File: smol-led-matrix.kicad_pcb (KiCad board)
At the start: 4 copper layers, 46.4 x 20.4 mm, 320 parts, among them J1 USB_C_Receptacle_USB2.0, J2 TagConnect_TC2030_SWD, Q1 FS8205, Q2 AO3401A, SW1 SW_Push, SW2 SW_Push, U1 STM32L433CBTx, U2 TP4054, U3 DW01+G, U4 XC6206P332MR

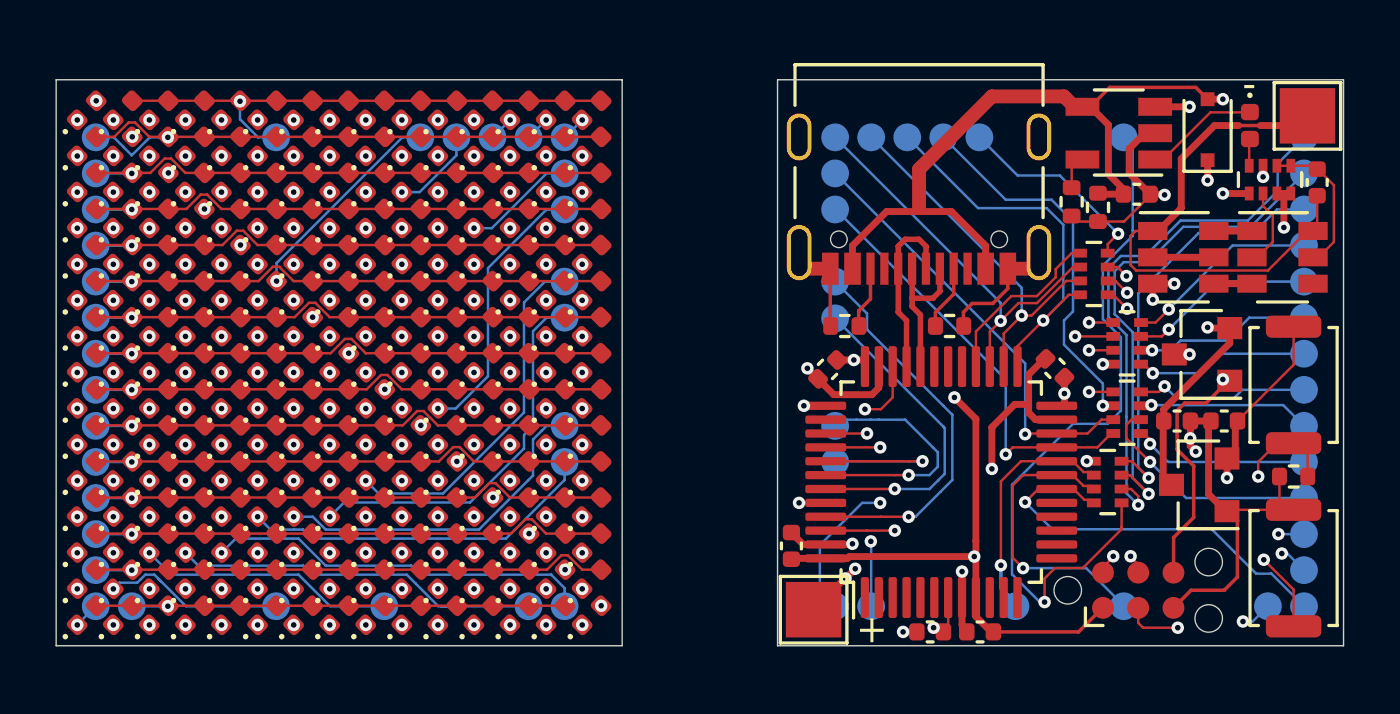
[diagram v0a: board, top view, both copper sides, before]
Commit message: Embed battery pads in plane for added mchanica rigidity
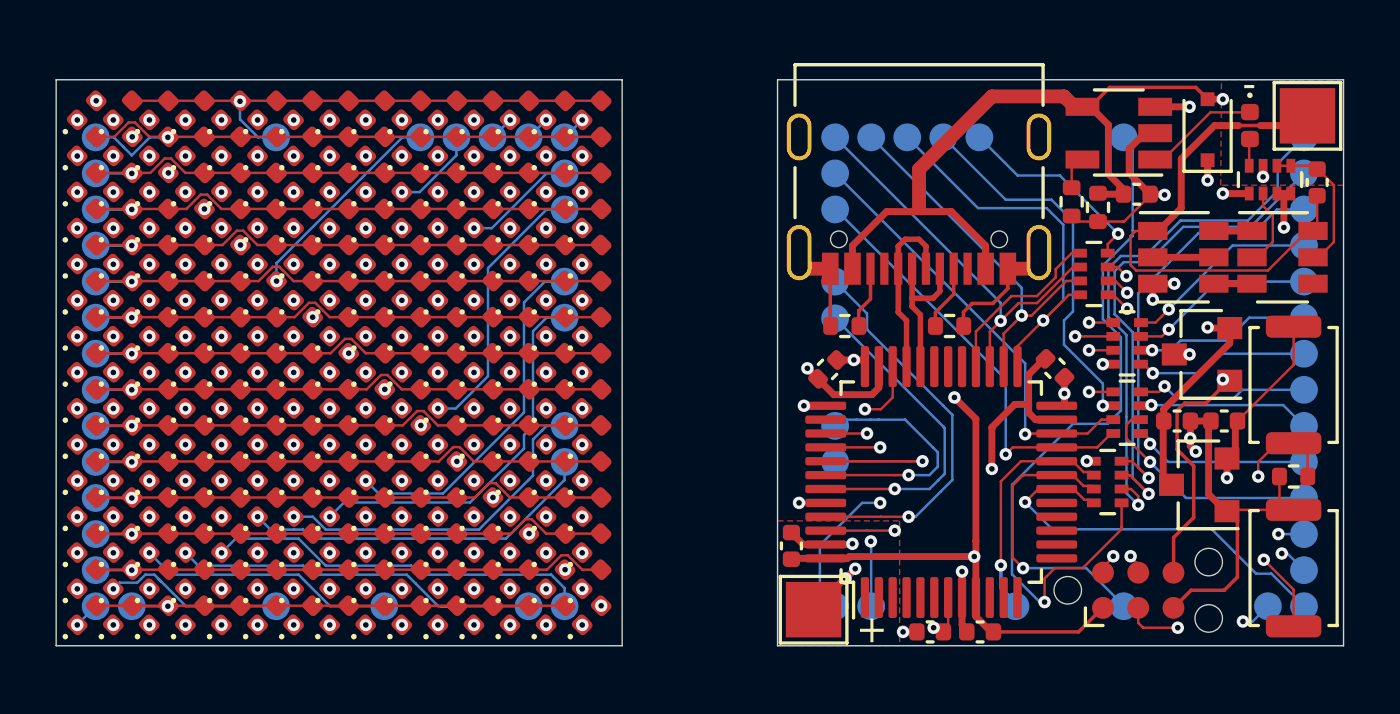
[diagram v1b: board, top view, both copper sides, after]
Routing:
- added copper zone on F.Cu, net +BATT
- added copper zone on F.Cu, net /Power/BAT-
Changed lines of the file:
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@@
     (user_trace_width 0.5)
     (trace_clearance 0.09)
-    (zone_clearance 0.508)
+    (zone_clearance 0.127)
     (zone_45_only no)
     (trace_min 0.09)
@@
       )
     )
+  )
+  (zone (net 66) (net_name +BATT) (layer F.Cu) (hatch edge 0.508)
+    (priority 10)
+    (connect_pads yes (clearance 0.127))
+    (min_thickness 0.127)
+    (fill yes (arc_segments 32) (thermal_gap 0.508) (thermal_bridge_width 0.508))
+    (polygon
+      (pts
+        (xy 129.975 117.975) (xy 125.575 117.975) (xy 125.575 113.475) (xy 129.975 113.475)
+      )
+    )
+  )
+  (zone (net 69) (net_name /Power/BAT-) (layer F.Cu) (hatch edge 0.508)
+    (priority 10)
+    (connect_pads yes (clearance 0.127))
+    (min_thickness 0.127)
+    (fill yes (arc_segments 32) (thermal_gap 0.508) (thermal_bridge_width 0.508))
+    (polygon
+      (pts
+        (xy 141.575 97.575) (xy 145.975 97.575) (xy 145.975 101.375) (xy 141.55 101.375)
+      )
+    )

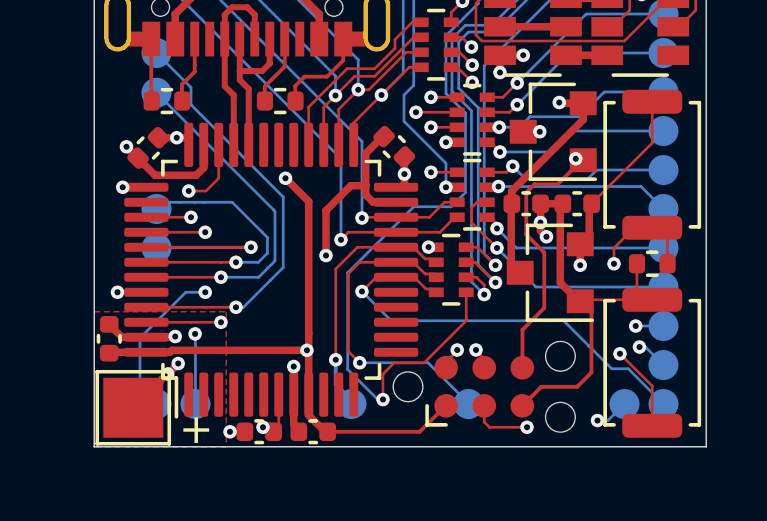
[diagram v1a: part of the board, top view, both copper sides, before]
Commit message: Bump up charge current to 45mA
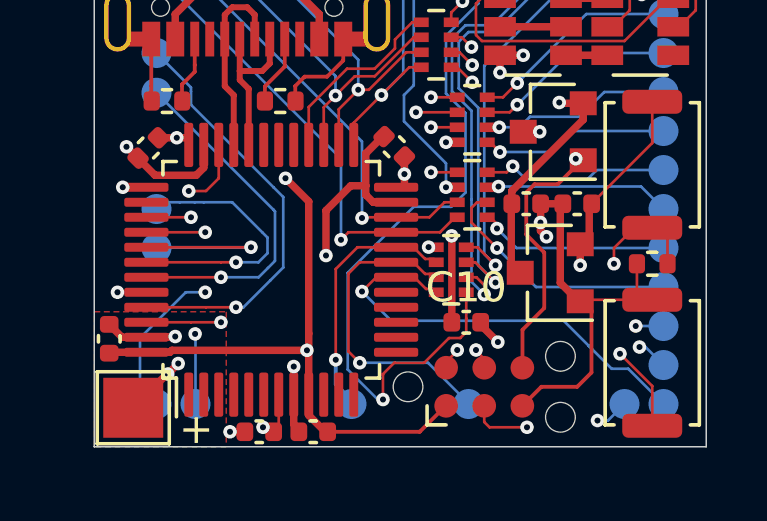
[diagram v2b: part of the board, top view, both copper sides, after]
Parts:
- added C10: 10uF, Capacitor_SMD:C_0402_1005Metric, F.Cu at (138.0, 113.8)
- R1: value 27kR -> 22kR
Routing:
- net GND: track 46.6 -> 49.4 mm, vias 11 -> 12
- net /A14: track 35.7 -> 37.0 mm
- net +3V3: track 46.9 -> 48.1 mm, vias 5 -> 6

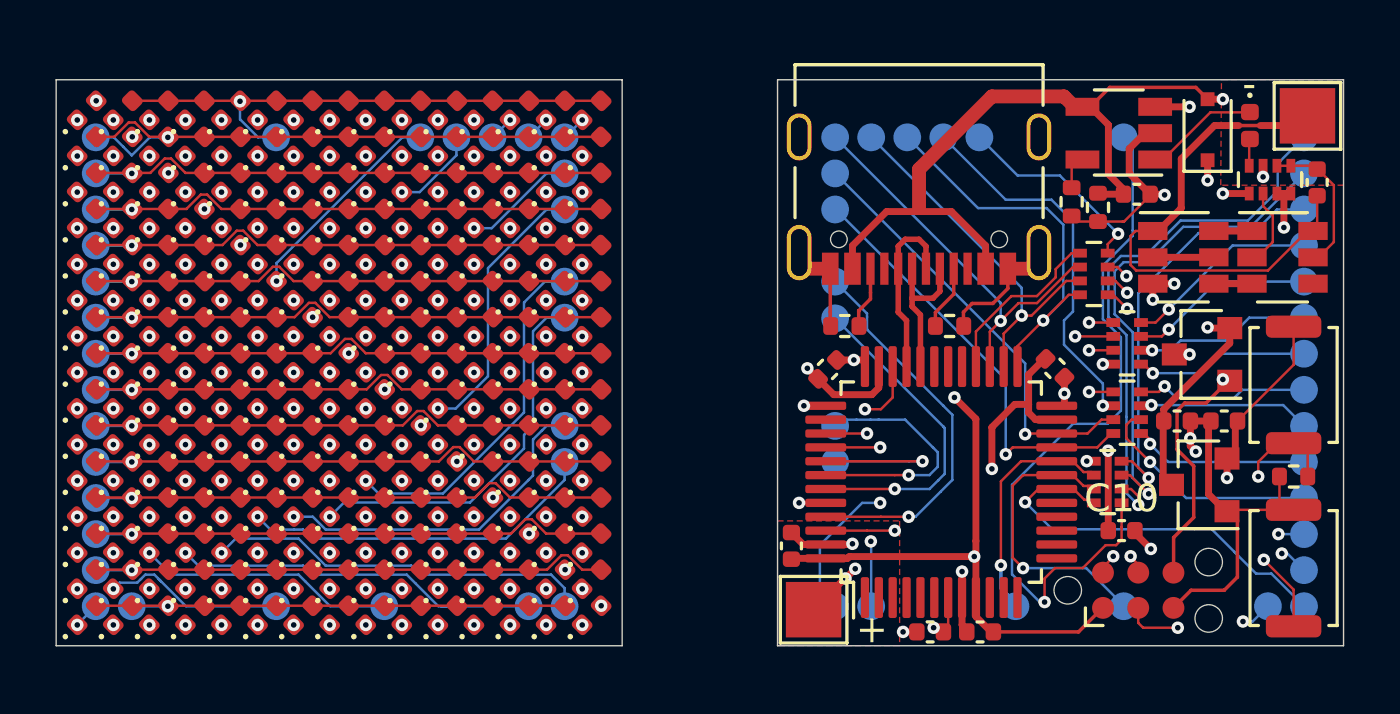
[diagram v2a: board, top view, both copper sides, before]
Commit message: Add charge current monitoring
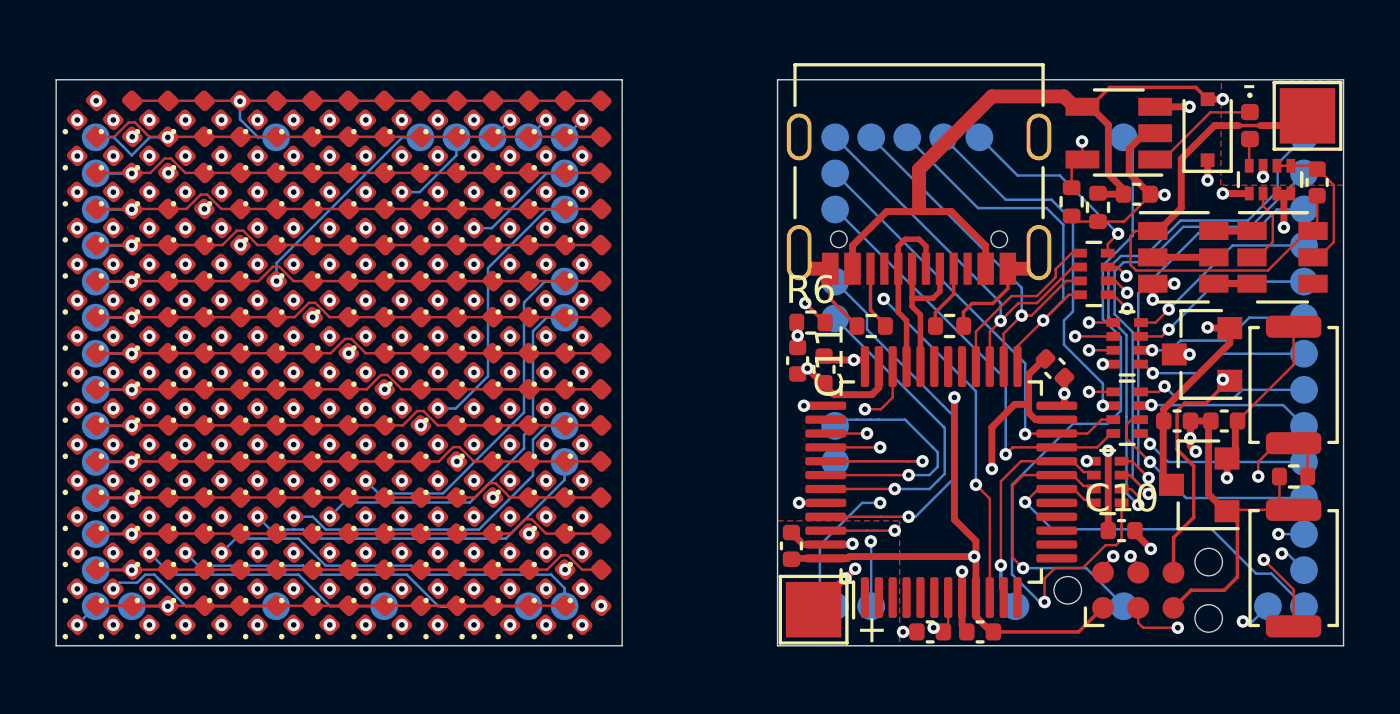
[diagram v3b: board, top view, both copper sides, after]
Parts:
- added C11: 100nF, Capacitor_SMD:C_0402_1005Metric, F.Cu at (126.3, 107.7)
- added R6: 22kR, Resistor_SMD:R_0402_1005Metric, F.Cu at (126.8, 106.3)
- R2, R5: value 27kR -> 22kR
- moved R4 0.95 mm to (128.9, 106.5)
- moved C8 0.12 mm to (127.2, 108.0), turned to 270 degrees
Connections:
- U1 pad 10: Net-(U1-Pad10) -> /I_chg
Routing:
- net /I_chg: track 0.00 -> 16.9 mm, vias 0 -> 3
- net Net-(R1-Pad1): track 1.06 -> 15.1 mm, vias 0 -> 2

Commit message: Hide silkscreen designators
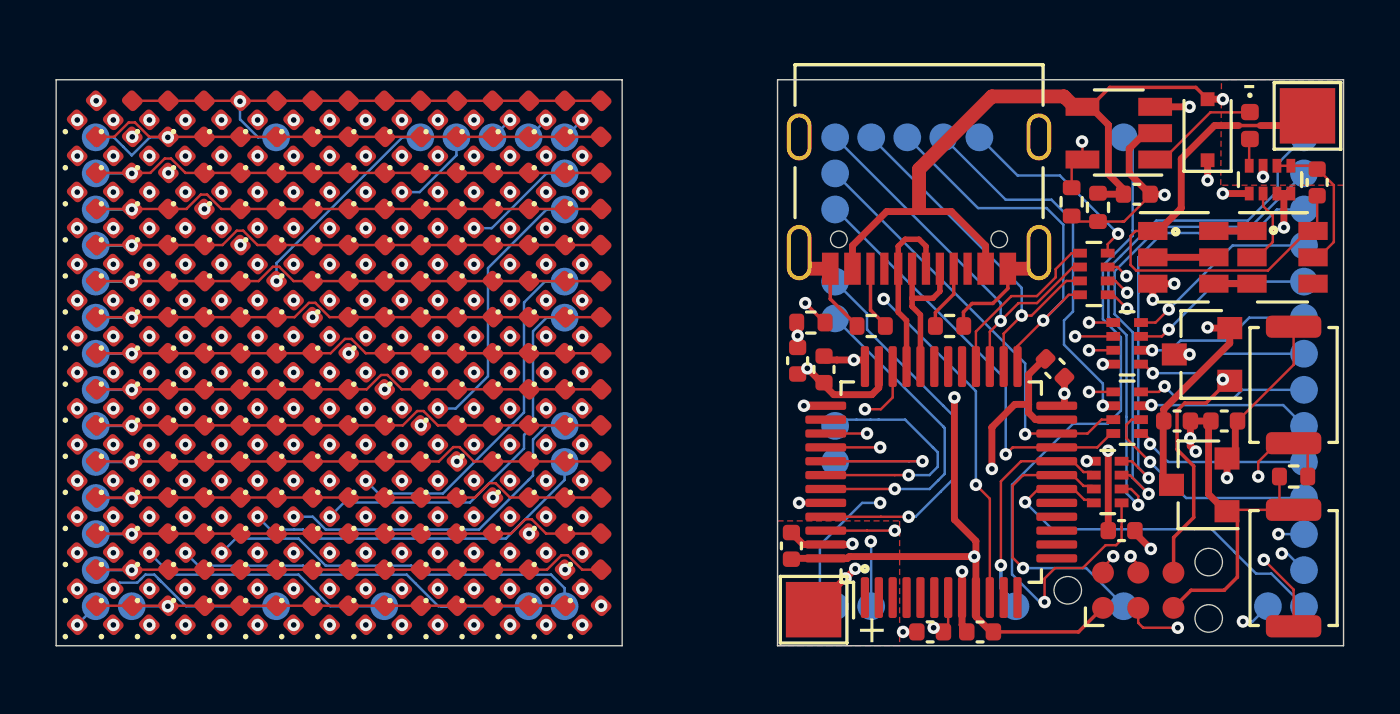
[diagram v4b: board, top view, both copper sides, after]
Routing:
- net /A3: track 35.2 -> 36.0 mm

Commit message: Break out BOOT0 to additional GPIO
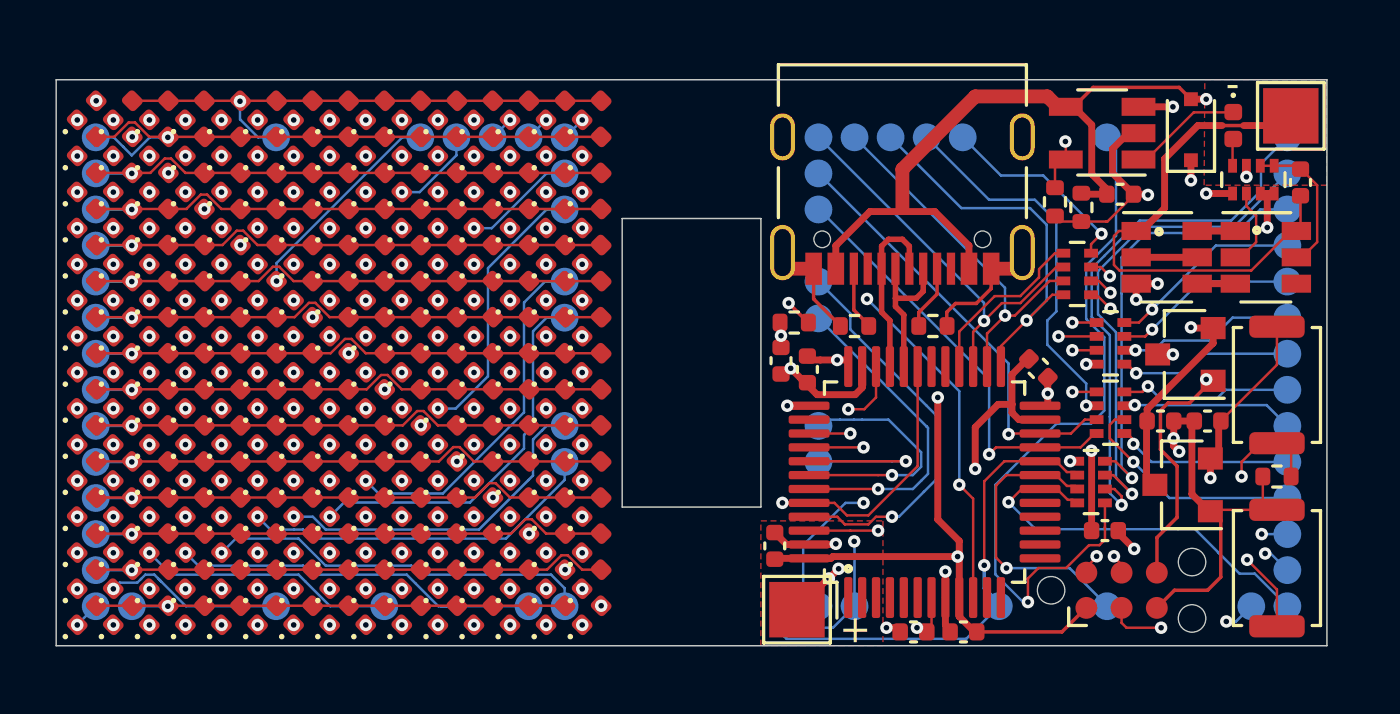
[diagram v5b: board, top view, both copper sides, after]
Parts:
- moved C7 0.60 mm to (141.1, 109.9)
- moved J1 0.60 mm to (130.1, 101.9)
- moved R1 0.60 mm to (135.6, 102.0)
- moved R5 0.60 mm to (143.6, 111.9)
- moved RN3 0.60 mm to (137.6, 107.1)
- moved RN4 0.60 mm to (137.6, 109.6)
- moved SW1 0.60 mm to (143.6, 108.6)
- moved SW2 0.60 mm to (143.6, 115.2)
- moved TP1 0.60 mm to (144.1, 98.9)
- moved TP34 0.60 mm to (137.4, 99.7)
- moved TP35 0.60 mm to (143.9, 99.7)
- moved TP36 0.60 mm to (143.9, 101.0)
- moved TP37 0.60 mm to (143.9, 102.2)
- moved TP38 0.60 mm to (143.9, 103.5)
- moved TP39 0.60 mm to (143.9, 104.8)
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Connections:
- U1 pad 31: Net-(U1-Pad31) -> /BOOT0
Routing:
- net /BOOT0: track 26.5 -> 34.9 mm
- net /K2: track 35.7 -> 44.0 mm
- net /K3: track 48.7 -> 51.3 mm
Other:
- board size 46.4 x 20.4 mm -> 45.8 x 20.4 mm
